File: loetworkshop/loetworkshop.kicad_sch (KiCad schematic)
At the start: 14 parts, among them SW1 SW_MEC_5E, SW2 SW_MEC_5E, SW3 SW_Push_SPDT, U1 CD40107BE, U2 NE555P

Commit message: Design board
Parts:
- BT1: footprint Resistor_THT:R_Axial_DIN0204_L3.6mm_D1.6mm_P1.90mm_Vertical -> Connector_PinHeader_2.54mm:PinHeader_1x02_P2.54mm_Vertical
- SW1: value SW_MEC_5E -> ON; footprint Button_Switch_THT:SW_PUSH_6mm -> switch_footprints:SW_PUSH_6mm
- SW2: value SW_MEC_5E -> OFF; footprint Button_Switch_THT:SW_PUSH_6mm -> switch_footprints:SW_PUSH_6mm
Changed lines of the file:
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@@
       (effects (font (size 1.27 1.27)) (justify left))
     )
-    (property "Value" "SW_MEC_5E" (id 1) (at 63.5 43.1799 90)
-      (effects (font (size 1.27 1.27)) (justify left))
-    )
-    (property "Footprint" "Button_Switch_THT:SW_PUSH_6mm" (id 2) (at 64.77 41.91 0)
+    (property "Value" "OFF" (id 1) (at 63.5 43.1799 90)
+      (effects (font (size 1.27 1.27)) (justify left))
+    )
+    (property "Footprint" "switch_footprints:SW_PUSH_6mm" (id 2) (at 64.77 41.91 0)
       (effects (font (size 1.27 1.27)) hide)
     )
@@
       (effects (font (size 1.27 1.27)) (justify left))
     )
-    (property "Value" "SW_MEC_5E" (id 1) (at 40.64 43.1799 90)
-      (effects (font (size 1.27 1.27)) (justify left))
-    )
-    (property "Footprint" "Button_Switch_THT:SW_PUSH_6mm" (id 2) (at 41.91 41.91 0)
+    (property "Value" "ON" (id 1) (at 40.64 43.1799 90)
+      (effects (font (size 1.27 1.27)) (justify left))
+    )
+    (property "Footprint" "switch_footprints:SW_PUSH_6mm" (id 2) (at 41.91 41.91 0)
       (effects (font (size 1.27 1.27)) hide)
     )
@@
       (effects (font (size 1.27 1.27)) (justify left))
     )
-    (property "Footprint" "Resistor_THT:R_Axial_DIN0204_L3.6mm_D1.6mm_P1.90mm_Vertical" (id 2) (at 20.32 26.416 90)
+    (property "Footprint" "Connector_PinHeader_2.54mm:PinHeader_1x02_P2.54mm_Vertical" (id 2) (at 20.32 26.416 90)
       (effects (font (size 1.27 1.27)) hide)
     )
@@
     )
     (path "/8fb675b2-23b6-4505-b26a-26135f1e4c68"
-      (reference "BT1") (unit 1) (value "Battery") (footprint "Resistor_THT:R_Axial_DIN0204_L3.6mm_D1.6mm_P1.90mm_Vertical")
+      (reference "BT1") (unit 1) (value "Battery") (footprint "Connector_PinHeader_2.54mm:PinHeader_1x02_P2.54mm_Vertical")
     )
     (path "/dcd29823-3fcc-4c07-9757-846194b63037"
@@
     )
     (path "/34d93e29-7670-4a9f-892b-6cc38920ddda"
-      (reference "SW1") (unit 1) (value "SW_MEC_5E") (footprint "Button_Switch_THT:SW_PUSH_6mm")
+      (reference "SW1") (unit 1) (value "ON") (footprint "switch_footprints:SW_PUSH_6mm")
     )
     (path "/23183067-079e-4704-86eb-8477ab8e7883"
-      (reference "SW2") (unit 1) (value "SW_MEC_5E") (footprint "Button_Switch_THT:SW_PUSH_6mm")
+      (reference "SW2") (unit 1) (value "OFF") (footprint "switch_footprints:SW_PUSH_6mm")
     )
     (path "/f3fb1339-bd6b-48ab-acdc-76d479ea27d8"

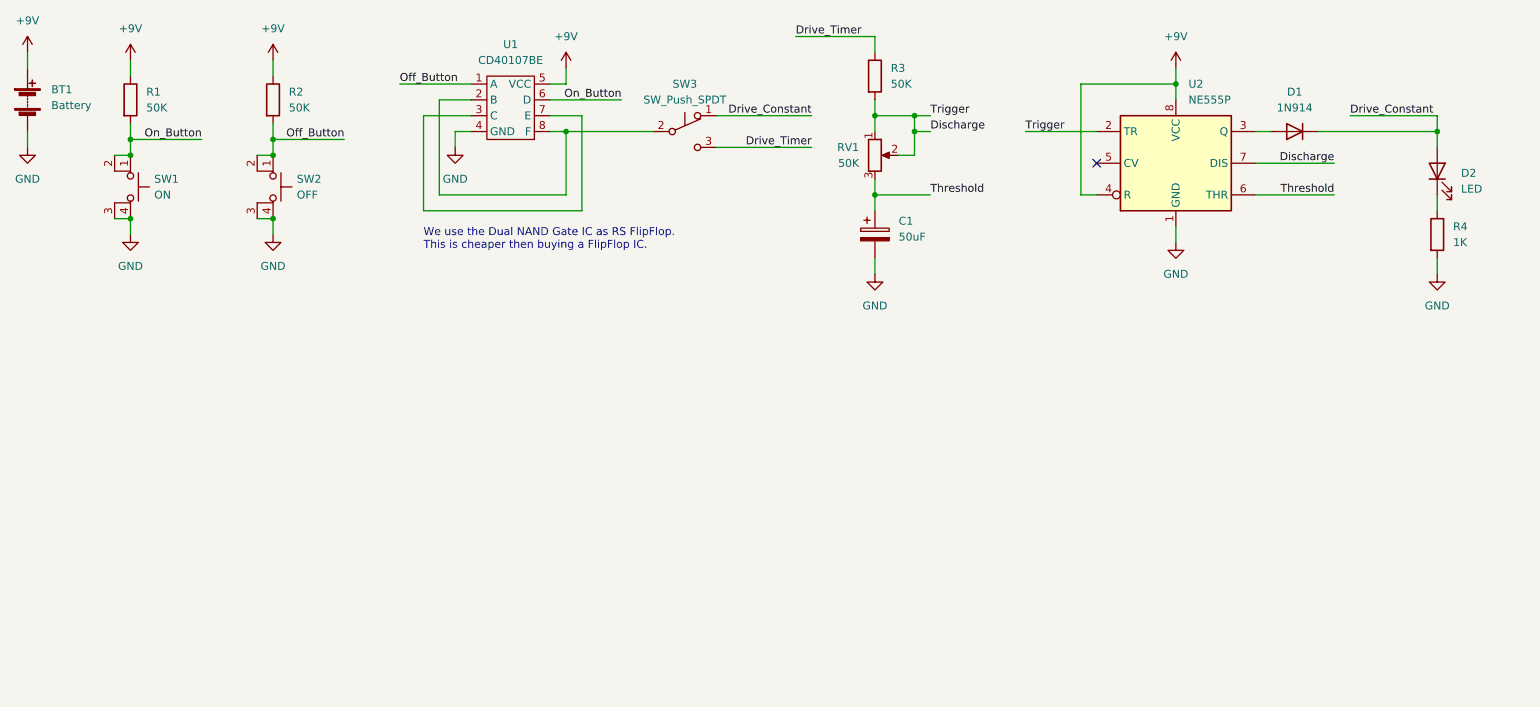
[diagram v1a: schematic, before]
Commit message: added third soldering challenge
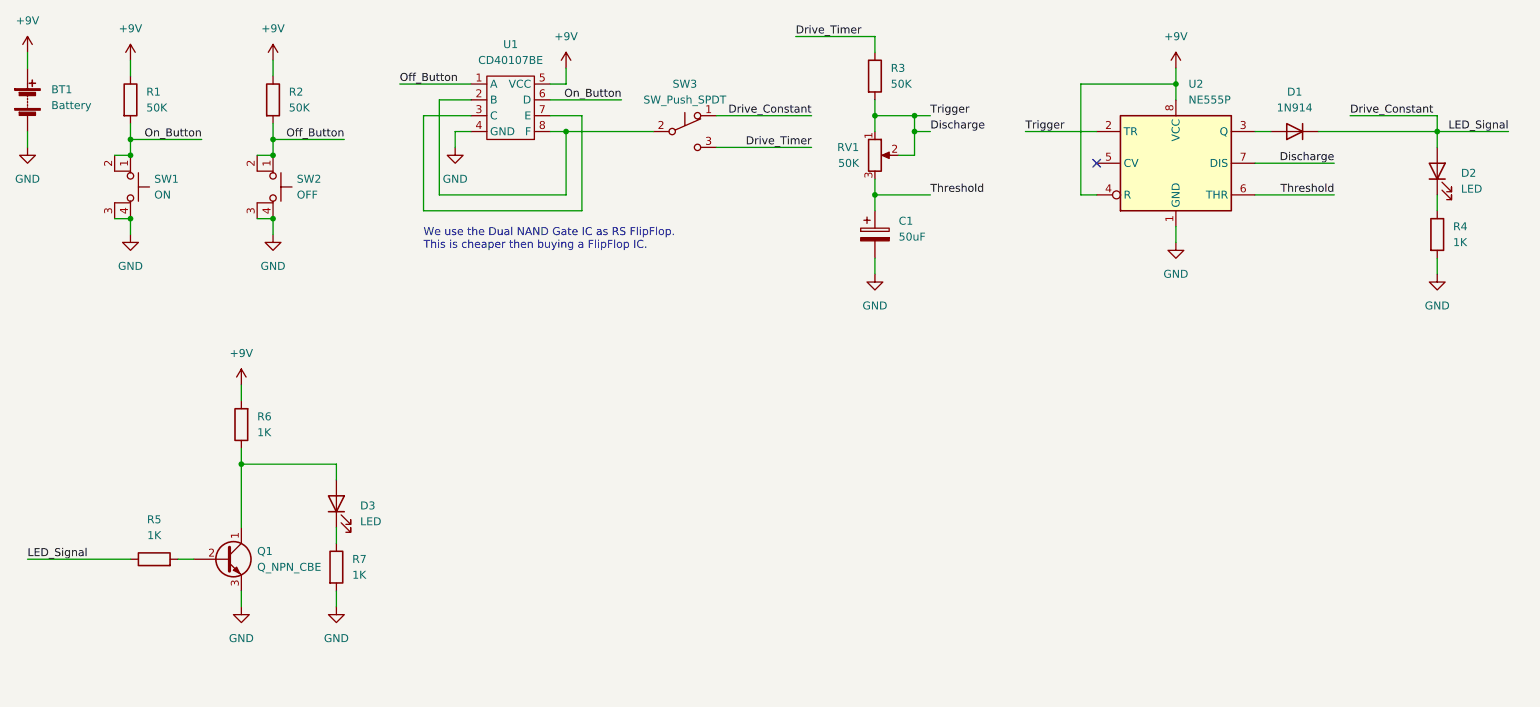
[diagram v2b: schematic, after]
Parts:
- added D3: LED, LED_THT:LED_D5.0mm, symbol Device:LED
- added Q1: Q_NPN_CBE, Package_TO_SOT_THT:TO-92, symbol Device:Q_NPN_CBE
- added R5, R6, R7: 1K, Resistor_THT:R_Axial_DIN0207_L6.3mm_D2.5mm_P7.62mm_Horizontal, symbol Device:R
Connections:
- net +9V: now also R6.2
- net Drive_Constant: now also R5.1
- net GND: now also Q1.3 (E), R7.2
- new net: Q1.2 (B), R5.2
- new net: D3.2 (A), Q1.1 (C), R6.1
- new net: D3.1 (K), R7.1

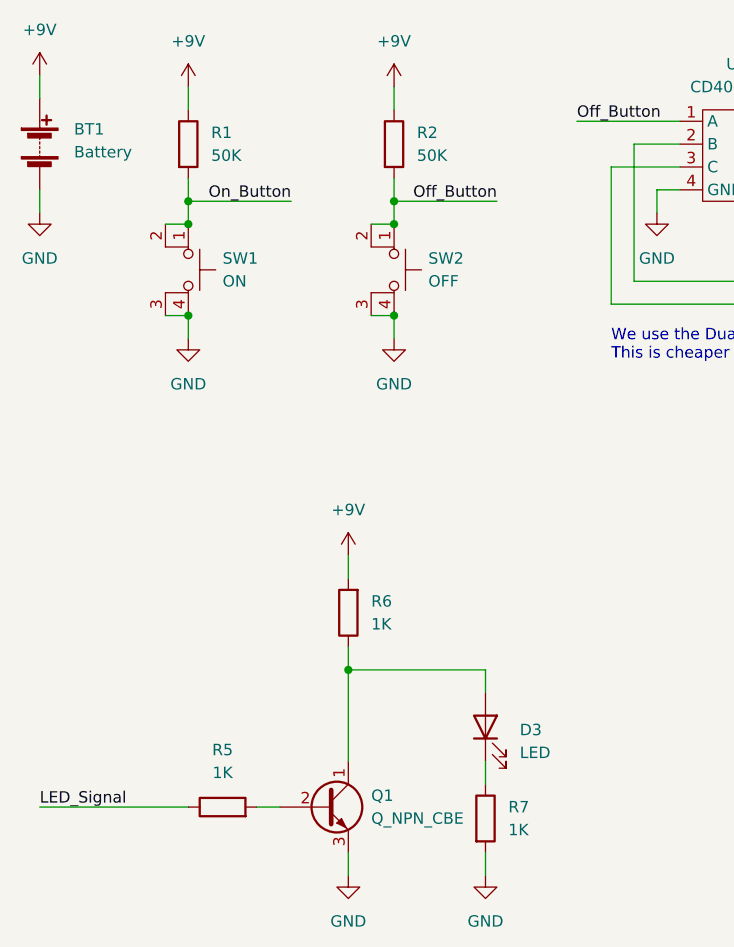
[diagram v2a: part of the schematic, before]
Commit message: new pcb layout
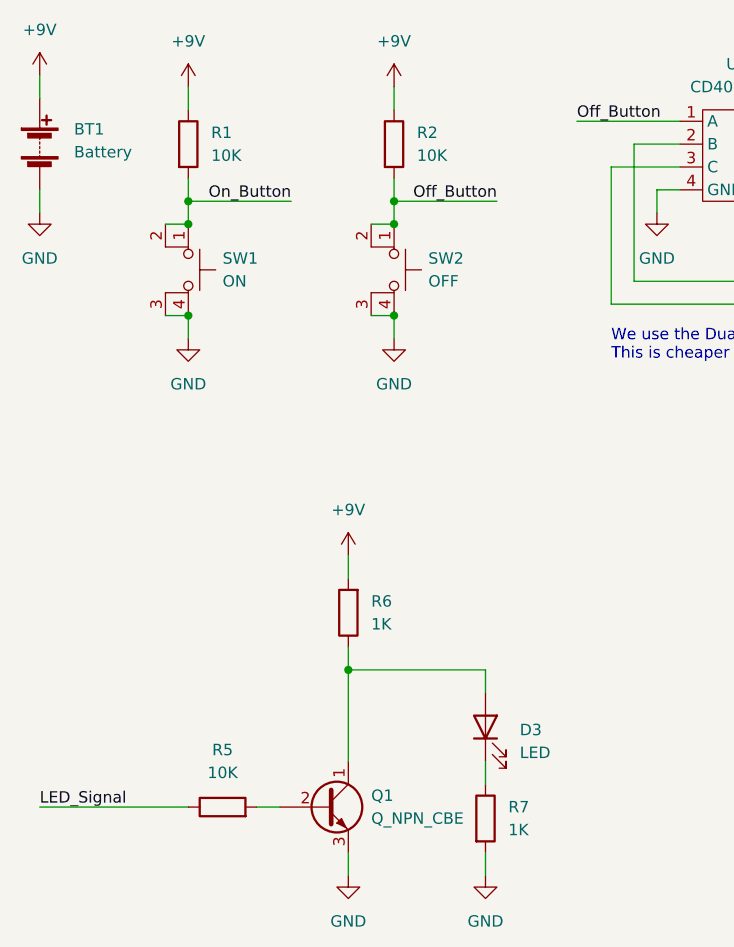
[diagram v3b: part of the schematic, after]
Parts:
- R1, R2: value 50K -> 10K
- R5: value 1K -> 10K
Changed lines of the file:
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@@
     (in_bom yes) (on_board yes) (fields_autoplaced)
     (property "Reference" "R5" (id 0) (at 40.64 95.25 90))
-    (property "Value" "1K" (id 1) (at 40.64 97.79 90))
+    (property "Value" "10K" (id 1) (at 40.64 97.79 90))
     (property "Footprint" "Resistor_THT:R_Axial_DIN0207_L6.3mm_D2.5mm_P7.62mm_Horizontal" (id 2) (at 40.64 103.378 90)
       (effects (font (size 1.27 1.27)) hide)
@@
       (effects (font (size 1.27 1.27)) (justify left))
     )
-    (property "Value" "50K" (id 1) (at 39.37 29.2099 0)
+    (property "Value" "10K" (id 1) (at 39.37 29.2099 0)
       (effects (font (size 1.27 1.27)) (justify left))
     )
@@
       (effects (font (size 1.27 1.27)) (justify left))
     )
-    (property "Value" "50K" (id 1) (at 62.23 29.2099 0)
+    (property "Value" "10K" (id 1) (at 62.23 29.2099 0)
       (effects (font (size 1.27 1.27)) (justify left))
     )
@@
     )
     (path "/18faa4c9-cc54-4d9f-b634-641f9d3c8724"
-      (reference "R1") (unit 1) (value "50K") (footprint "Resistor_THT:R_Axial_DIN0207_L6.3mm_D2.5mm_P7.62mm_Horizontal")
+      (reference "R1") (unit 1) (value "10K") (footprint "Resistor_THT:R_Axial_DIN0207_L6.3mm_D2.5mm_P7.62mm_Horizontal")
     )
     (path "/419f44d7-d555-4706-99ac-733c18a90197"
-      (reference "R2") (unit 1) (value "50K") (footprint "Resistor_THT:R_Axial_DIN0207_L6.3mm_D2.5mm_P7.62mm_Horizontal")
+      (reference "R2") (unit 1) (value "10K") (footprint "Resistor_THT:R_Axial_DIN0207_L6.3mm_D2.5mm_P7.62mm_Horizontal")
     )
     (path "/9e14dd43-0fb7-4e60-92a4-f58637916ead"
@@
     )
     (path "/071488e9-807f-4b64-9d5c-31f601fa1699"
-      (reference "R5") (unit 1) (value "1K") (footprint "Resistor_THT:R_Axial_DIN0207_L6.3mm_D2.5mm_P7.62mm_Horizontal")
+      (reference "R5") (unit 1) (value "10K") (footprint "Resistor_THT:R_Axial_DIN0207_L6.3mm_D2.5mm_P7.62mm_Horizontal")
     )
     (path "/852f923a-6f83-443e-b67c-6e60cc704666"

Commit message: rev 1.1 - fixed IC Pinout in the Footprint
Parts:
- U1: footprint Package_DIP:DIP-8_W7.62mm -> switch_footprints:DIP-8_W7.62mm_InvertedDualRow
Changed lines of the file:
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@@
     (property "Reference" "U1" (id 0) (at 97.79 19.05 0))
     (property "Value" "CD40107BE" (id 1) (at 97.79 21.59 0))
-    (property "Footprint" "Package_DIP:DIP-8_W7.62mm" (id 2) (at 97.79 22.86 0)
+    (property "Footprint" "switch_footprints:DIP-8_W7.62mm_InvertedDualRow" (id 2) (at 97.79 22.86 0)
       (effects (font (size 1.27 1.27)) hide)
     )
@@
     )
     (path "/8bd678c5-38de-4e07-96ae-b7ff455294d0"
-      (reference "U1") (unit 1) (value "CD40107BE") (footprint "Package_DIP:DIP-8_W7.62mm")
+      (reference "U1") (unit 1) (value "CD40107BE") (footprint "switch_footprints:DIP-8_W7.62mm_InvertedDualRow")
     )
     (path "/3f06ceca-2295-4774-9307-7bda35753381"

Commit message: rev 1.2
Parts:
- U1: footprint switch_footprints:DIP-8_W7.62mm_InvertedDualRow -> Package_DIP:DIP-8_W7.62mm
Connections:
- net +9V: now also U1.8 (VCC); no longer U1.5 (VCC)
- net On_Button: now also U1.7 (D); no longer U1.6 (D)
- net at SW3.2 (B), U1.2 (B): now also U1.5 (F); no longer U1.8 (F)
- net at U1.3 (C): now also U1.6 (E); no longer U1.7 (E)
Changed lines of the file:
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@@
     (property "Reference" "U1" (id 0) (at 97.79 19.05 0))
     (property "Value" "CD40107BE" (id 1) (at 97.79 21.59 0))
-    (property "Footprint" "switch_footprints:DIP-8_W7.62mm_InvertedDualRow" (id 2) (at 97.79 22.86 0)
+    (property "Footprint" "Package_DIP:DIP-8_W7.62mm" (id 2) (at 97.79 22.86 0)
       (effects (font (size 1.27 1.27)) hide)
     )
@@
     )
     (path "/8bd678c5-38de-4e07-96ae-b7ff455294d0"
-      (reference "U1") (unit 1) (value "CD40107BE") (footprint "switch_footprints:DIP-8_W7.62mm_InvertedDualRow")
+      (reference "U1") (unit 1) (value "CD40107BE") (footprint "Package_DIP:DIP-8_W7.62mm")
     )
     (path "/3f06ceca-2295-4774-9307-7bda35753381"

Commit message: rev 1.3 - more footprint fixes
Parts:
- U2: footprint Package_DIP:DIP-8_W7.62mm -> switch_footprints:DIP-8_W7.62mm_InvertedDualRow
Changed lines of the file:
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@@
       (effects (font (size 1.27 1.27)) (justify left))
     )
-    (property "Footprint" "Package_DIP:DIP-8_W7.62mm" (id 2) (at 220.98 48.26 0)
+    (property "Footprint" "switch_footprints:DIP-8_W7.62mm_InvertedDualRow" (id 2) (at 220.98 48.26 0)
       (effects (font (size 1.27 1.27)) hide)
     )
@@
     )
     (path "/3f06ceca-2295-4774-9307-7bda35753381"
-      (reference "U2") (unit 1) (value "NE555P") (footprint "Package_DIP:DIP-8_W7.62mm")
-    )
-  )
+      (reference "U2") (unit 1) (value "NE555P") (footprint "switch_footprints:DIP-8_W7.62mm_InvertedDualRow")
+    )
+  )

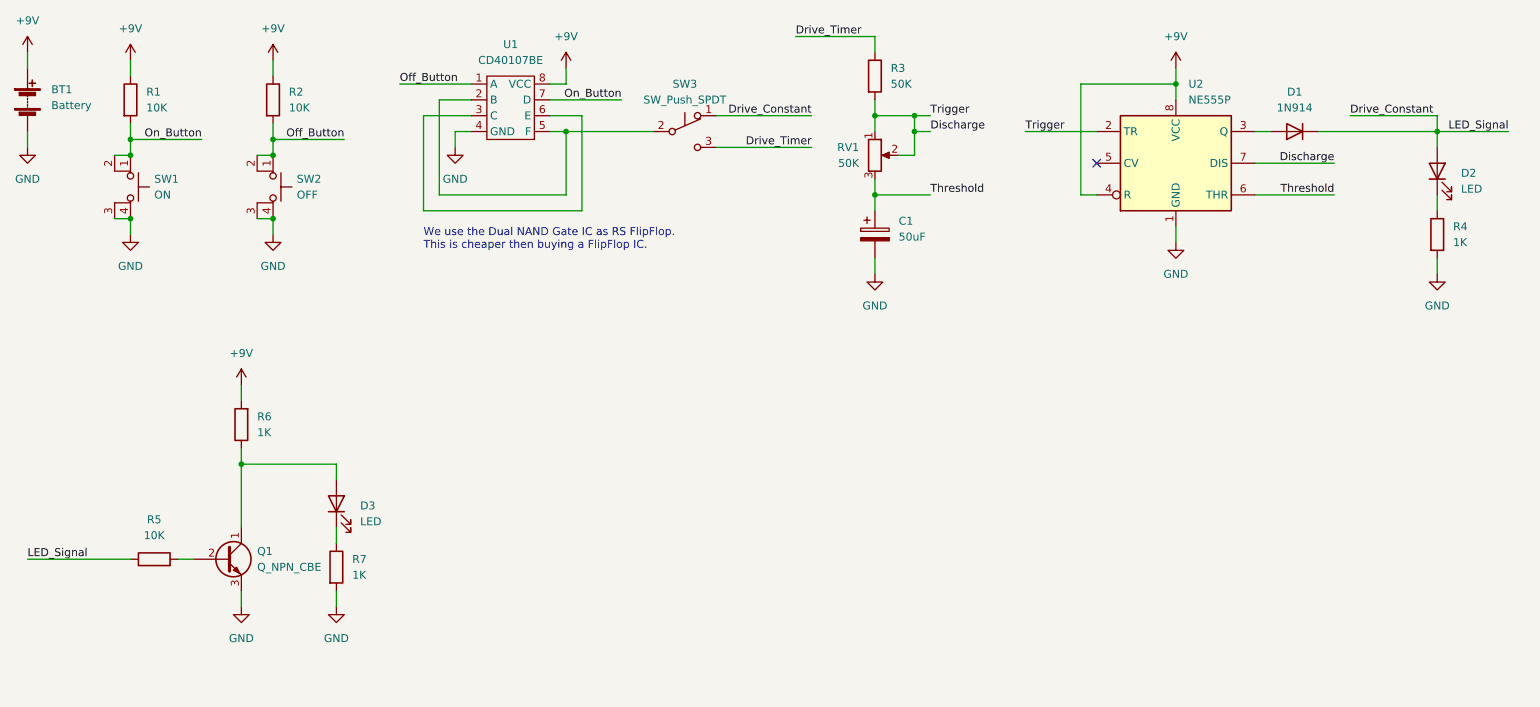
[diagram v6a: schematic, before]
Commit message: Changes to accomodate issues in NAND Driver Design
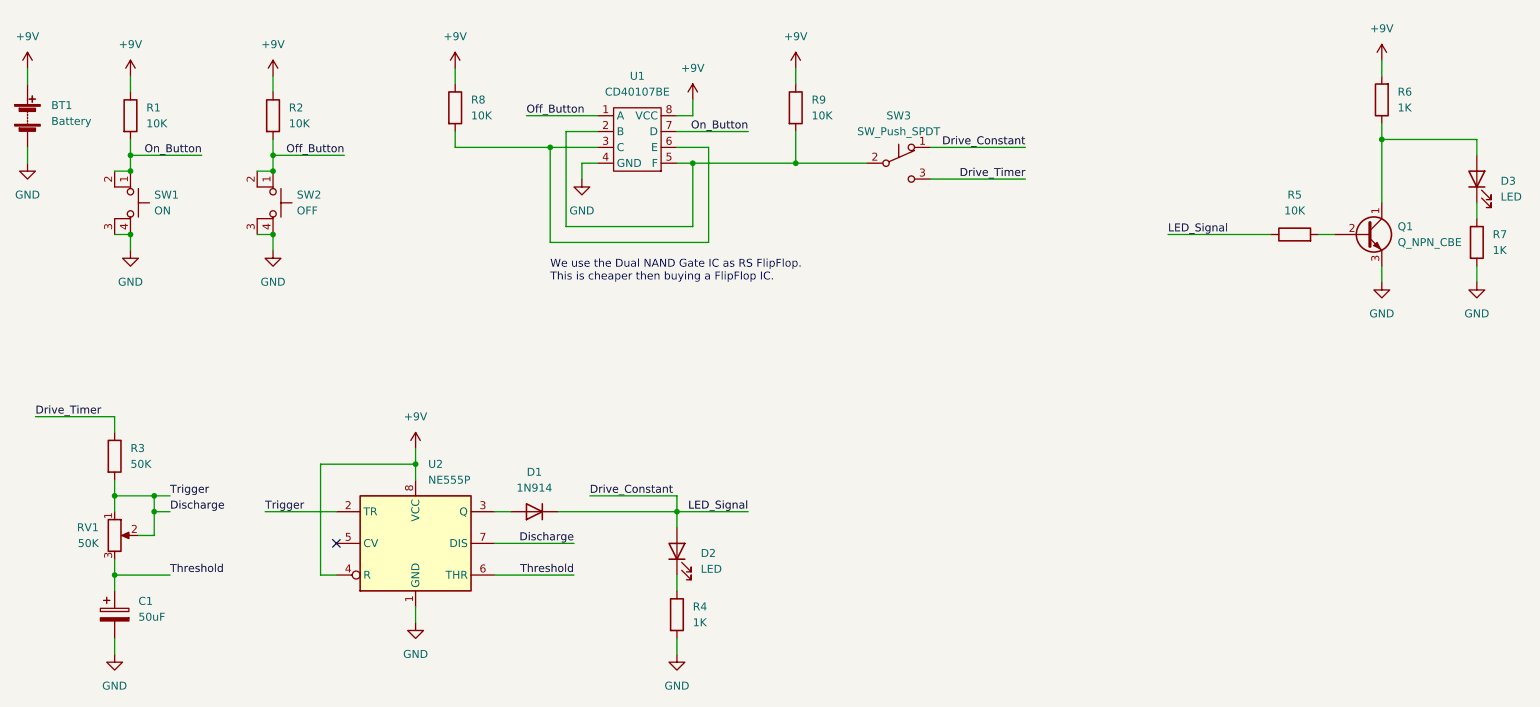
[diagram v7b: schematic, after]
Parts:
- added R8, R9: 10K, Resistor_THT:R_Axial_DIN0207_L6.3mm_D2.5mm_P7.62mm_Horizontal, symbol Device:R
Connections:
- net +9V: now also R8.1, R9.1
- net at SW3.2 (B), U1.2 (B), U1.5 (F): now also R9.2
- net at U1.3 (C), U1.6 (E): now also R8.2
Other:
- moved on the sheet: BT1, C1, D1, D2, D3, Q1, R1, R2, R3, R4, R5, R6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
